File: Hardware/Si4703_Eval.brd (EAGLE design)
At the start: 22.9 x 31.8 mm, 38 parts, among them U1 SI4703, U3 TPA6111, Y1 32.768kHz

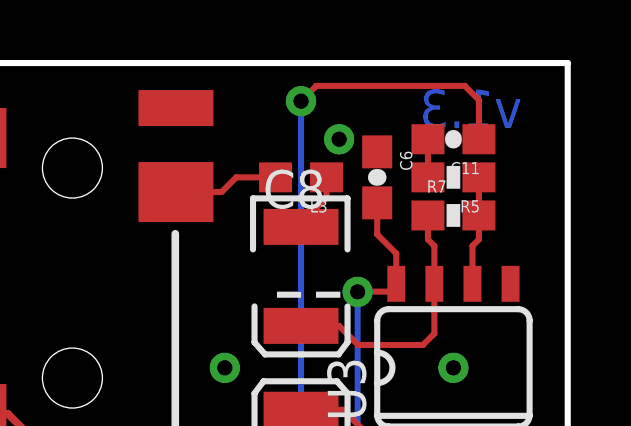
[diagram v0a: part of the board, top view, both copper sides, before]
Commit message: Fixing review complaints on version number and upside down ground on schematic
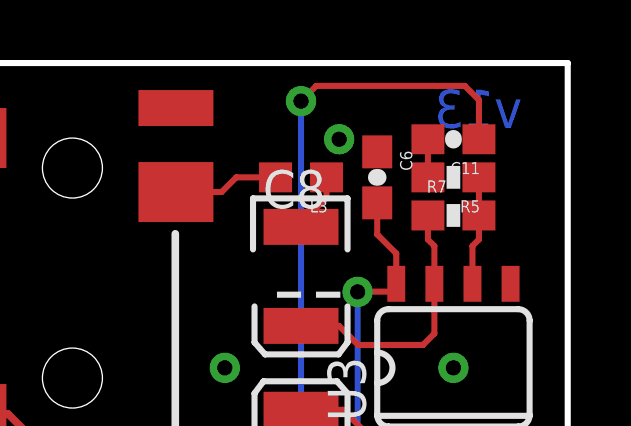
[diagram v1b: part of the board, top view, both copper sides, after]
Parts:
- moved U$1 31.8 mm to (-1.27, -11.4)
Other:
- board text added: "Toni Klopfenstein"
- board text added: "v13"
- board text removed: "v1.3"

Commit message: created panel v13
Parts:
- moved JP5 2.54 mm to (1.27, 24.1)
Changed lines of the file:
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@@
 <?xml version="1.0" encoding="utf-8"?>
 <!DOCTYPE eagle SYSTEM "eagle.dtd">
-<eagle version="6.5.0">
+<eagle version="6.6.0">
 <drawing>
 <settings>
@@
 <setting verticaltext="up"/>
 </settings>
-<grid distance="0.05" unitdist="inch" unit="inch" style="lines" multiple="1" display="yes" altdistance="0.005" altunitdist="inch" altunit="inch"/>
+<grid distance="0.05" unitdist="inch" unit="inch" style="lines" multiple="1" display="yes" altdistance="0.01" altunitdist="inch" altunit="inch"/>
 <layers>
 <layer number="1" name="Top" color="4" fill="1" visible="yes" active="yes"/>
@@
 <layer number="18" name="Vias" color="2" fill="1" visible="yes" active="yes"/>
 <layer number="19" name="Unrouted" color="6" fill="1" visible="yes" active="yes"/>
-<layer number="20" name="Dimension" color="15" fill="1" visible="yes" active="yes"/>
-<layer number="21" name="tPlace" color="16" fill="1" visible="yes" active="yes"/>
-<layer number="22" name="bPlace" color="14" fill="1" visible="yes" active="yes"/>
+<layer number="20" name="Dimension" color="6" fill="1" visible="yes" active="yes"/>
+<layer number="21" name="tPlace" color="6" fill="1" visible="yes" active="yes"/>
+<layer number="22" name="bPlace" color="6" fill="1" visible="yes" active="yes"/>
 <layer number="23" name="tOrigins" color="15" fill="1" visible="yes" active="yes"/>
 <layer number="24" name="bOrigins" color="15" fill="1" visible="yes" active="yes"/>
@@
 <element name="JP3" library="SparkFun" package="SFE-LOGO-FLAME" value="LOGO-SFESK" x="19.8908" y="5.3543"/>
 <element name="JP4" library="SparkFun" package="FIDUCIAL-1X2" value="FIDUCIAL1X2" x="21.59" y="3.81"/>
-<element name="JP5" library="SparkFun" package="FIDUCIAL-1X2" value="FIDUCIAL1X2" x="1.27" y="26.67"/>
+<element name="JP5" library="SparkFun" package="FIDUCIAL-1X2" value="FIDUCIAL1X2" x="1.27" y="24.13"/>
 <element name="U4" library="SparkFun-Connectors" package="AUDIO-JACK-3.5MM-SMD" value="" x="6.35" y="31.75" rot="R270"/>
 <element name="FRAME2" library="SparkFun-Aesthetics" package="CREATIVE_COMMONS" value="FRAME-LETTER" x="-12.7" y="-8.89"/>
